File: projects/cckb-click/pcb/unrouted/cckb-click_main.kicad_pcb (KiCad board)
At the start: 2 copper layers, 291.2 x 100.7 mm, 184 parts, among them SW1 SKRAAWE010, SW10 SKRAAWE010, SW11 SKRAAWE010, SW12 SKRAAWE010, SW13 SKRAAWE010, SW14 SKRAAWE010, SW15 SKRAAWE010, SW16 SKRAAWE010, SW17 SKRAAWE010, SW18 SKRAAWE010, SW19 SKRAAWE010, SW2 SKRAAWE010, SW20 SKRAAWE010, SW21 SKRAAWE010, SW22 SKRAAWE010, SW23 SKRAAWE010, SW24 SKRAAWE010, SW25 SKRAAWE010, SW26 SKRAAWE010, SW27 SKRAAWE010, SW28 SKRAAWE010, SW29 SKRAAWE010, SW3 SKRAAWE010, SW30 SKRAAWE010, SW31 SKRAAWE010, SW32 SKRAAWE010, SW33 SKRAAWE010, SW34 SKRAAWE010, SW35 SKRAAWE010, SW36 SKRAAWE010, SW37 SKRAAWE010, SW38 SKRAAWE010, SW39 SKRAAWE010, SW4 SKRAAWE010, SW40 SKRAAWE010, SW41 SKRAAWE010, SW42 SKRAAWE010, SW43 SKRAAWE010, SW44 SKRAAWE010, SW45 SKRAAWE010, SW46 SKRAAWE010, SW47 SKRAAWE010, SW48 SKRAAWE010, SW49 SKRAAWE010, SW5 SKRAAWE010, SW50 SKRAAWE010, SW51 SKRAAWE010, SW52 SKRAAWE010, SW53 SKRAAWE010, SW54 SKRAAWE010, SW55 SKRAAWE010, SW56 SKRAAWE010, SW57 SKRAAWE010, SW58 SKRAAWE010, SW59 SKRAAWE010, SW6 SKRAAWE010, SW60 SKRAAWE010, SW61 SKRAAWE010, SW62 SKRAAWE010, SW7 SKRAAWE010, SW8 SKRAAWE010, SW9 SKRAAWE010, U1 SN74LVC595APWR, U2 SN74LVC595APWR

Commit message: cckb-click: 枠とキャップ・組み立ての立体・配線した基板（DRC 違反 0・未配線 0・警告 0）
枠と基板は spec.py を共有するので 1 つのコミットにした。

- 枠 2 枚（左 156.4・右 140.0）とキャップ 62 個（click_case.py）。基板の下から M2×4 を 20 本、枠の壁に直にねじ込む。
  電池は手前の壁の口から出し入れ・USB は左奥・電源スイッチは右の縁
- 組み立ての立体で干渉（置く・押し切る・傾ける）・下から入れられるか・電池を出せるか・サポート無しで刷れるかを検査
  （tests/test_cckb_click_case.py。各検査に、故意に壊すと落ちる検査）
- 配線: 行・列・595 からの束・電池からの電源は決まった形（click_routes.py）。残りは Freerouting 2.3.0（tools/route_click.py）
- 板の検査（tests/test_cckb_click_board.py）: DRC・JLC の寸法・禁止域・GND のビアまでの距離・発注道具の出力（BOM 7 行・CPL 133 行）
- たわみ（click_stiffness.py）: リブの断面は作った枠を切って測る（式は 2.8、枠は 2.64 だった → 10 N で 0.086・余裕 0.1）
- 電池クリップの −に裏へのビアを 3 個・電源スイッチの端子のランドを LCSC の中心に

projects/cckb/ は変えていない。

Co-Authored-By: Claude Opus 5.5 (1M context) <noreply@anthropic.com>
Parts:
- added TP_VSW: TP_VBAT_SW, TestPoint_Pad_D1.0mm, F.Cu at (29.0, 128.3)
- moved U2 164.9 mm to (20.5, 119.0), turned to -90 degrees
- moved C_U2 158.4 mm to (24.7, 124.4)
- moved H25 21.3 mm to (138.3, 100.0)
- moved H26 21.3 mm to (195.5, 100.0)
- moved H27 21.3 mm to (233.6, 100.0)
- moved H24 21.3 mm to (81.2, 100.0)
- moved D43 16.1 mm to (45.9, 124.6)
- moved D_PWR 15.0 mm to (11.6, 112.6)
- moved C_U1 12.3 mm to (40.9, 124.4)
- moved R_HI 2.50 mm to (13.9, 124.0), turned to 180 degrees
- moved R_LO 2.30 mm to (10.1, 124.0), turned to 180 degrees
- turned U1 to -90 degrees

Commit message: cckb-click: 1 回目の監査の直し（基板を配線し直した・枠・ねじの試し刷り・ファーム・検査）
基板（DRC 違反 0・未配線 0・警告 0。sha256 4dc68901…）
- 電池は止めに当たる所に座る（クリップの原点から 0.51 奥）。表の銅を置かない範囲を奥へ広げた: 缶の縁から銅まで 0 → 0.72
- 載せないコンデンサのランド 2 つ（C_BAT = VBAT_SW–GND・C_3V3 = V3V3–GND。1206 と 0805 が載る・JLC は実装しない・ペースト無し）
- 手前の継ぎ目の両側に予備のねじ穴 2 つ。外周のねじ穴を 0.1 外へ（穴の縁から基板の縁まで 1.0）
- パスコンの GND から 595 の GND までを GND の線で引く（31.6 → 22.3 mm）・595 の本体の下の帯に線を通さずビアを先に打つ
  （表の GND のいちばん遠い所 17.2 → 13.3 mm）・電池電圧の線を行の線から 1.8 離す・C_3V3 への線を決まった形で
- 試験用のランドのシルクの輪・ランドの中のビアの禁止・アンテナの禁止域の手前の細い帯を塗らない・DRC の下限をビア φ0.6・穴 0.3 に

枠
- ねじの所の厚い壁を ±2.0 に（下穴のまわりの肉 0.49 → 0.71。幅の広いキーの脇の 3 本は 0.49 のまま）・予備のねじの下穴
- 電源スイッチと XIAO の逃げをパッドの外接 ＋ 0.4 に・指の切り欠きの奥行き 4.5
- ねじの試し刷り coupon_screw_plate（本番の枠から切り出した壁 2 つ ＋ 厚さ 1.6 の当て板。3 番だけ壁を 0.5 厚くした）

ファーム: SPI の MISO（D9・基板では空き）にプルダウン（ボードの pinctrl の写しと突き合わせ）

検査（どれも壊すと落ちる）: 電池の縁から表の銅まで・シルクの図形とマスクの開口・戻りの道のり・電池電圧の線と行の線・
ランドが 0805 と 1206 の標準の足跡を含む・電池クリップの向き（CPL・JLC の部品データの外形）・電池電圧の式・ねじの肉 22 か所・
枠とパッドの隙・ねじの試し刷りが本番の枠と同じ形。全検査 655 passed。

Co-Authored-By: Claude Opus 5.5 (1M context) <noreply@anthropic.com>
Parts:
- added C_3V3: cap_land_unpopulated, C_1206_0805_Land, F.Cu at (53.1, 121.5)
- added C_BAT: cap_land_unpopulated, C_1206_0805_Land, F.Cu at (287.2, 133.0)
- added H28: Hole_M2_2.2, Hole_M2_2.2, F.Cu at (148.3, 148.2)
- added H29: Hole_M2_2.2, Hole_M2_2.2, F.Cu at (161.3, 148.2)
- moved H18 0.10 mm to (293.5, 77.2)
- moved H19 0.10 mm to (293.5, 119.0)
- moved H0 0.10 mm to (16.6, 51.8)
- moved H1 0.10 mm to (54.8, 51.8)
- moved H2 0.10 mm to (92.8, 51.8)
- moved H3 0.10 mm to (130.9, 51.8)
- moved H4 0.10 mm to (150.0, 51.8)
- moved H5 0.10 mm to (169.1, 51.8)
- moved H6 0.10 mm to (207.2, 51.8)
- moved H7 0.10 mm to (245.2, 51.8)
- moved H8 0.10 mm to (283.4, 51.8)
- moved H16 0.10 mm to (6.53, 77.2)
- moved H17 0.10 mm to (6.53, 115.2)
- moved H10 0.10 mm to (104.8, 148.2)
- moved H11 0.10 mm to (140.5, 148.2)
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
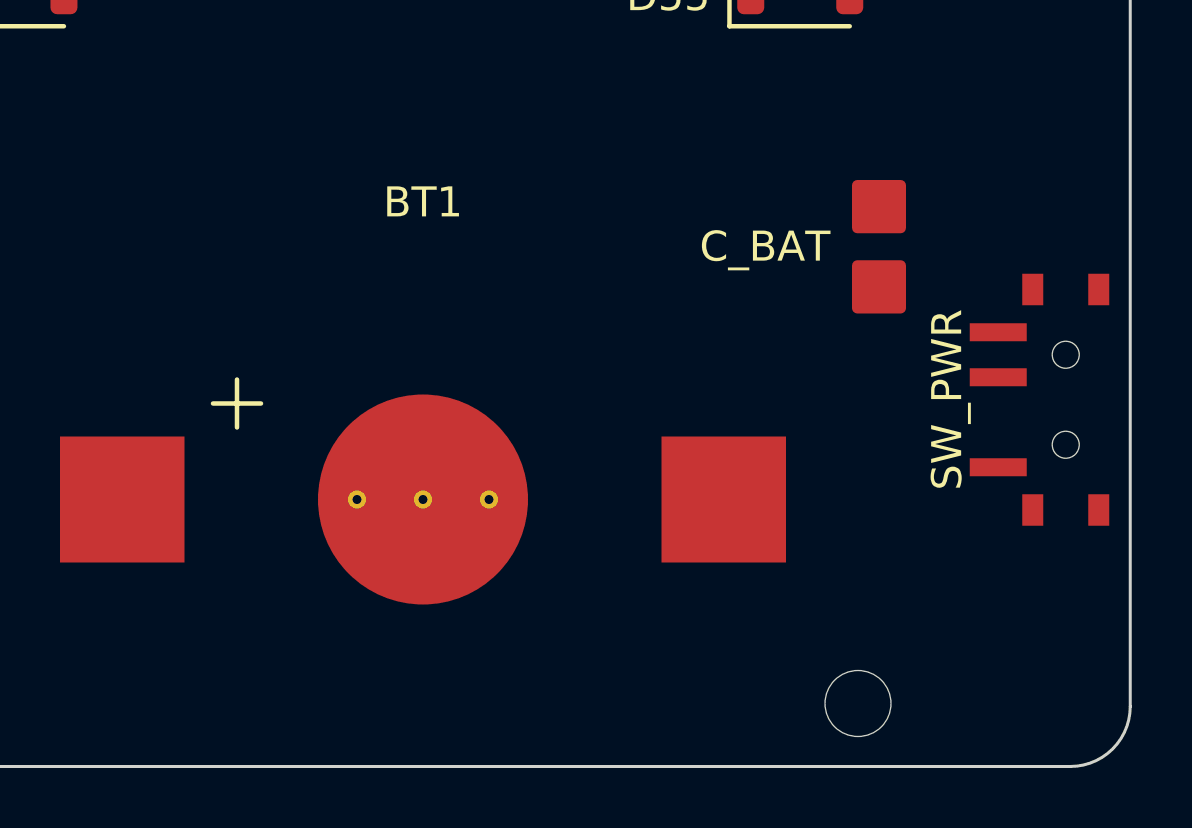
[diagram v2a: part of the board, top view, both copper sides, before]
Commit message: cckb-click: 電源スイッチを基板の縁から 2.5 内側へ・つまみの切り欠き・差し込み式の電池の蓋・蓋のねじ穴・角の試し刷り
利用者の決定（2026-10-04）:
- 電源スイッチ MSK12C02 を 1.75 内側へ（本体は縁から 2.50 = JLC の規約・つまみの先は枠の外面の 1.35 内側）。
  枠の右の壁を幅 10・上まで切り欠き、内側は屋根を厚くして塞ぐ。入の向きと印は同じ
- 電池の蓋（cover_battery.stl）: L 字・手前から滑らせる・枠のひさしと溝だけで留まる・無くても使える
- 蓋のねじ穴 H30・H31（非めっき φ2.2・使わない）。電池クリップのコートヤードの口の側の両脇を欠いた
- 角の試し刷り（coupon_corner_plate.stl）: 本番の枠の右手前の角 ＋ 当て板 ＋ つまみ・電池の代わり ＋ 蓋

基板: C_BAT を 1.0 左へ。電池の＋（VBAT_IN）を決まった形に。SPI・595 どうし・電源の枝は、監査した板（4dc68901…）で
Freerouting が引いた線を pcb/freerouted.json から置き直す（引くたびに形が変わらない）。右手前の角の外で前の板と違うのは
VBAT_SW の長い線の右の端だけ。DRC 違反 0・未配線 0・警告 0。板 fe90b1e6…

検査（それぞれ壊すと落ちる）: 本体と縁 2.5・つまみが枠の内側・爪の入る場所・蓋が当たらず滑って抜けて留まる・
蓋のねじ穴と裏の銅・置き直した線が記録と同じ・角の試し刷りが本番の枠と同じ。全検査 677 passed。

Co-Authored-By: Claude Opus 5.5 (1M context) <noreply@anthropic.com>
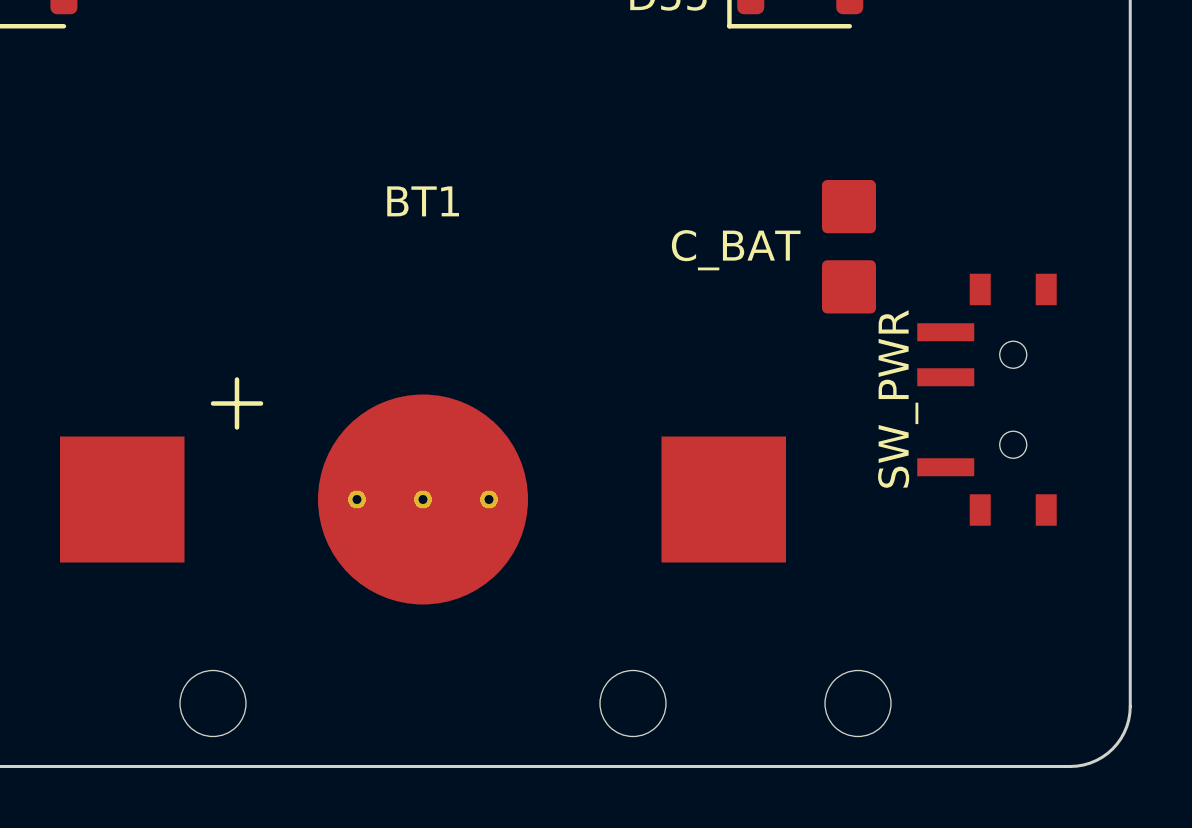
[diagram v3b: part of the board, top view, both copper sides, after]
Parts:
- added H30: Hole_M2_2.2, Hole_M2_2.2, F.Cu at (265.0, 148.2)
- added H31: Hole_M2_2.2, Hole_M2_2.2, F.Cu at (279.0, 148.2)
- moved SW_PWR 1.75 mm to (291.1, 138.1)
- moved C_BAT 1.00 mm to (286.2, 133.0)

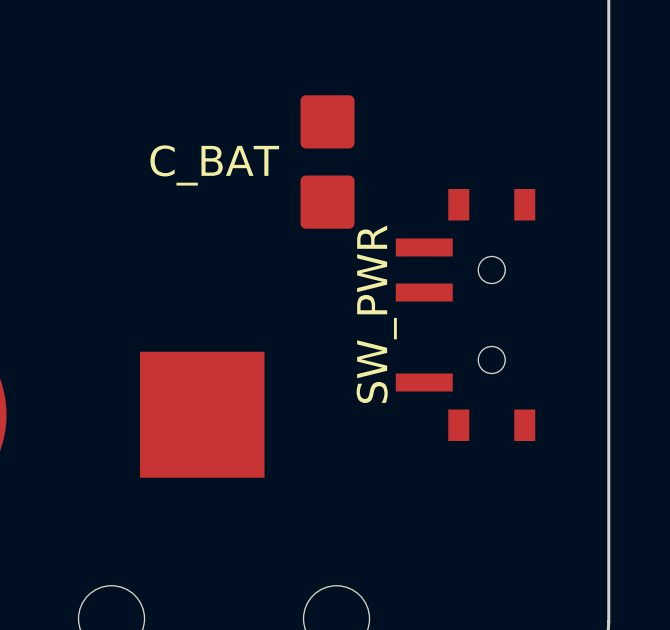
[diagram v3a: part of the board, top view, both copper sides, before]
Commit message: cckb-click: 試し刷り v2 の結果を本番へ（電源スイッチを 0.75 外へ・切り欠きを利用者が触った形に・下穴 φ1.6・蓋を刷る物から外す）
利用者が試し刷り v2 を刷って決めた（2026-10-04）:
- 電源スイッチ: (ii) 0.75 外。本体は基板の縁から 1.75・つまみの先は基板の縁の 0.30 内・枠の外面の 0.60 内。
  JLC の実装の規約「本体と縁は 2.5 mm 以上」は満たさない（規約より使いやすさ）
- 基板: SW_PWR だけ動かし、角だけ引き直した。角の外の違いは VBAT_SW の長い線の右の端 0.75 だけ。
  DRC 違反 0・未配線 0・警告 0。板 b442b865…。入の向き（端子の網）は同じ
- 枠: 切り欠きは外面へ片側 2.4 広がり、内側の上の縁を 2.0 斜めに（PSW_NOTCH）。入の印は斜面のすぐ内の平らな上面へ。
  下穴 φ1.6（22 個とも。薄い壁も補正しない: 線で 1.50 = 利用者が締めた切れ端と同じ）
- 電池の蓋: 4 つとも使えなかった。刷る物・組んだ絵から外した（枠の口のまわりの形と基板の穴 H30・H31 は前のまま）
- 検査: 「本体が縁から 2.5 以上」を、決めた決まり（つまみの先が縁の 0.30 以上内側・枠から出ない・本体 1.75 を記録）に置き換えた。
  最初の位置・0.1 外・前の位置で落ちる。下穴の径・指先の球・切り欠きの縁の強さ（断面を立体から測る）を足した
- 道具: 本番の枠の下穴 22 個を G-code で測る（tools/slice_main.py）
- 試し刷り v2 は、刷った物と同じ形を出し続ける（位置を本番から測り直した）

Co-Authored-By: Claude Opus 5.5 (1M context) <noreply@anthropic.com>
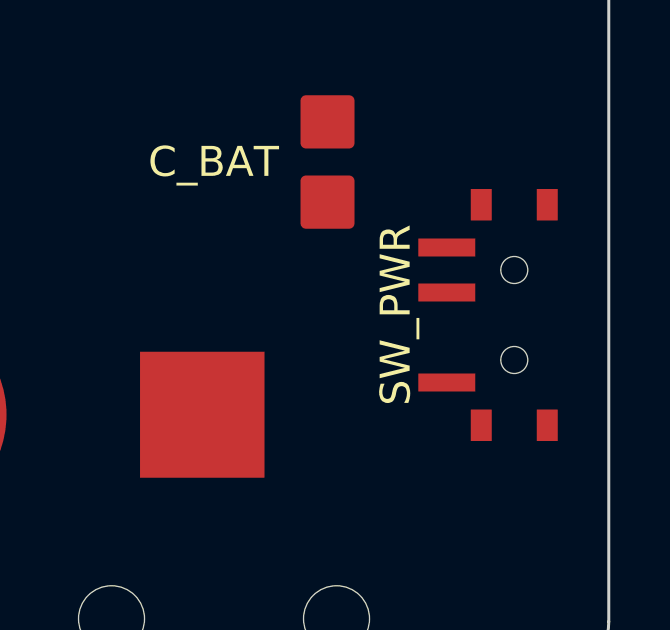
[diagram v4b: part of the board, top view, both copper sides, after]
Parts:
- moved SW_PWR 0.75 mm to (291.9, 138.1)
